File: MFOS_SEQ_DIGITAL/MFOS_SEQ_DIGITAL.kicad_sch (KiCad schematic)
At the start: 181 parts, among them J1 Conn_01x01, J10 Conn_01x01, J11 Conn_01x01, J12 Conn_01x01, J13 Conn_01x01, J14 Conn_01x01, J15 Conn_01x01, J16 Conn_01x01, J17 Conn_01x01, J18 Conn_01x01, J19 Conn_01x01, J2 Conn_01x01, J20 Conn_01x01, J21 Conn_01x01, J22 Conn_01x01, J23 Conn_01x01, J24 Conn_01x01, J25 Conn_01x01, J26 Conn_01x01, J27 Conn_01x01, J28 Conn_01x01, J29 Conn_01x01, J3 Conn_01x01, J30 Conn_01x01, J4 Conn_01x01, J5 Conn_01x01, J6 Conn_01x01, J7 Conn_01x01, J8 Conn_01x01, J9 Conn_01x01, Q1 2N3904, U1 40106, U2 40106, U3 4013, U4 40193, U5 4514, U6 40106, U7 TL082, U8 HC4094

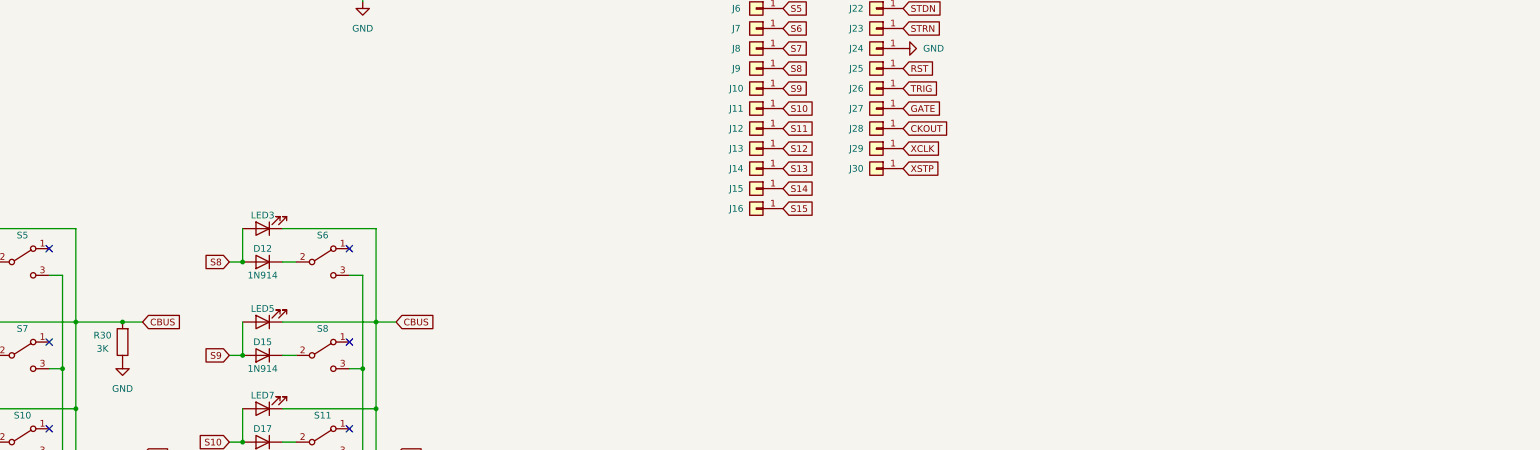
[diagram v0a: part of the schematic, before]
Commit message: Updated BOM, renamed VCO > MFOS_VCO
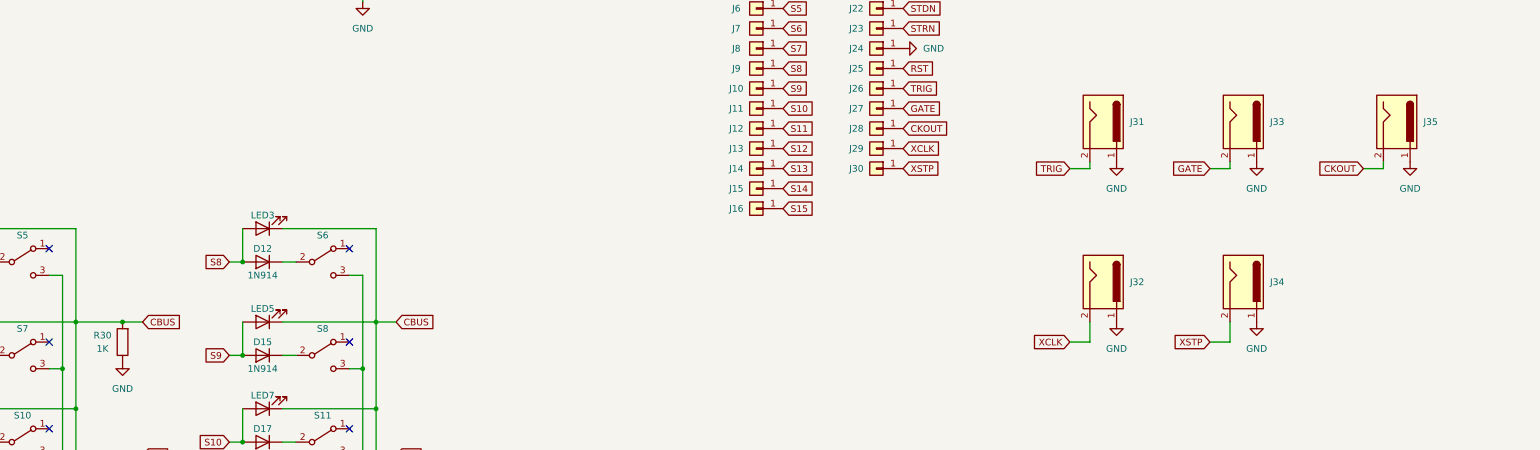
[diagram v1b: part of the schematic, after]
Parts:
- added J31, J32, J33, J34, J35: Jack-DC, symbol Connector:Jack-DC
- R30: value 3K -> 1K
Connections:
- net CKOUT: now also J35.2
- net GATE: now also J33.2
- net GND: now also J31.1, J32.1, J33.1, J34.1, J35.1
- net TRIG: now also J31.2
- net XCLK: now also J32.2
- net XSTP: now also J34.2

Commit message: Reviewed BOM
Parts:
- C10: symbol Device:C_Polarized -> dhk:C_Tantalum
- J1, J10, J11, J12, J13, J14, J15, J16, J17, J18, J19, J2, J20, J21, J22, J23, J24, J25, J26, J27, J28, J29, J3, J30, J4, J5, J6, J7, J8, J9: now left out of the parts list
- S12: value SW_DPDT_x2 -> DPDT
- S25: value SW_Rotary1x4 -> SP4T
- S9: value SW_Rotary12 -> SP12T
